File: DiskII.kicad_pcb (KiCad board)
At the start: 2 copper layers, 100 x 77.5 mm, 35 parts, among them J1 Apple II Expansion Slot, J2 DRIVE 2, J3 DRIVE 1, Q1 2N3906, Q2 MPSU51, Q3 MPSU51

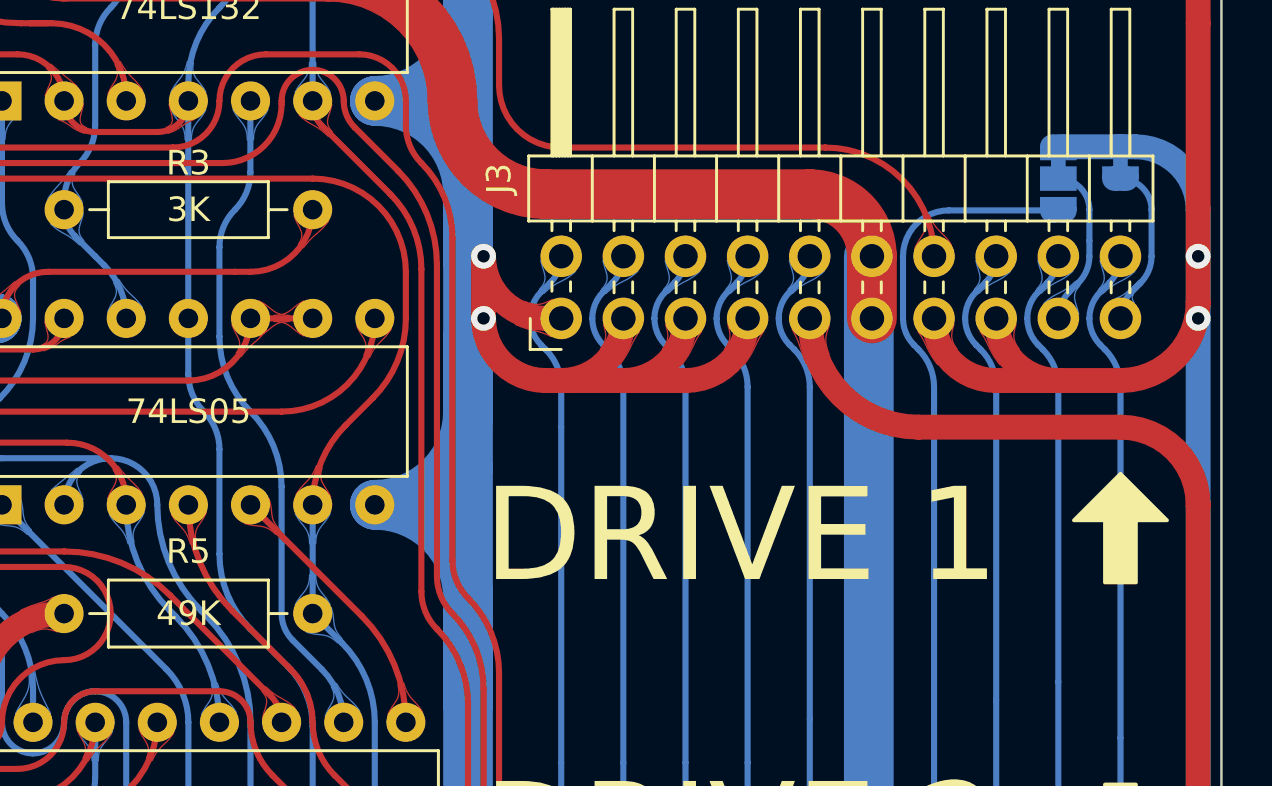
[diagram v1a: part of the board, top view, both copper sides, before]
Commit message: jumper to put WPROT on pin 19
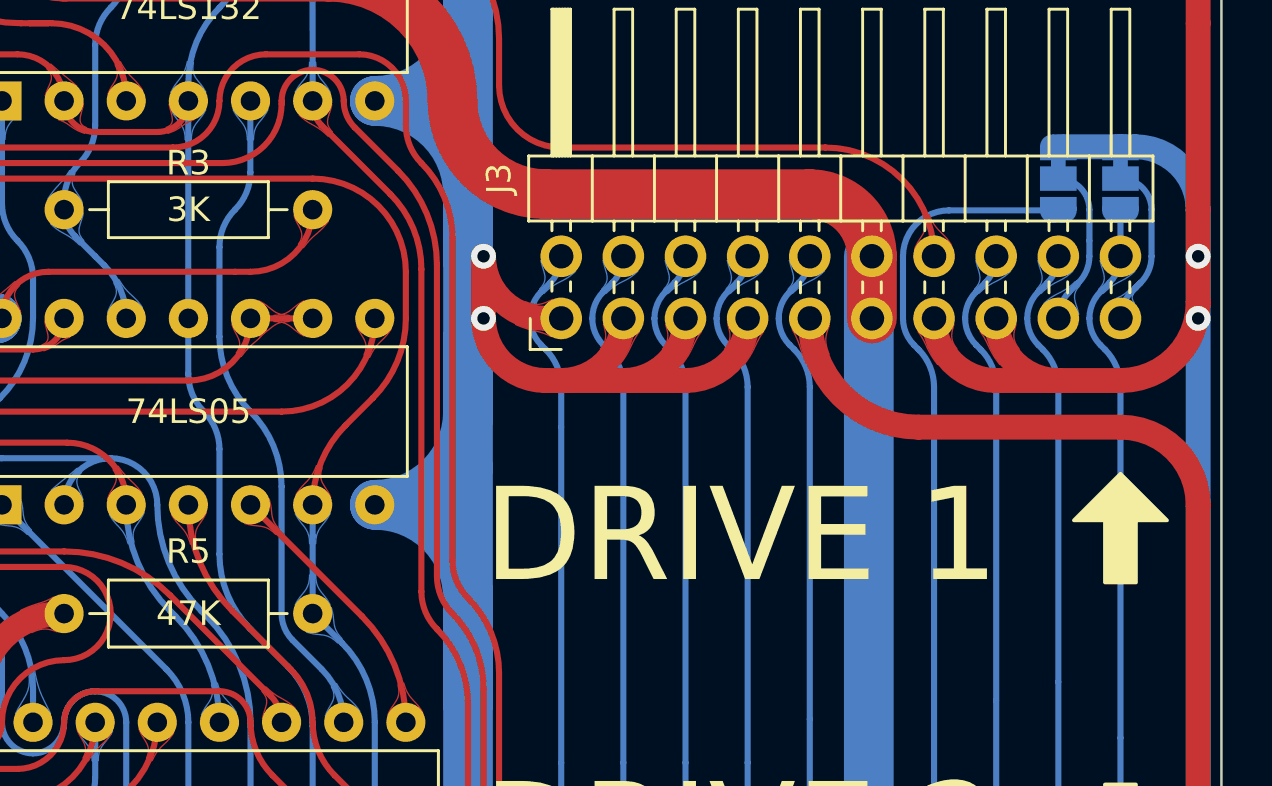
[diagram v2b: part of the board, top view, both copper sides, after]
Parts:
- JP19: footprint Jumper:SolderJumper-2_P1.3mm_Bridged_RoundedPad1.0x1.5mm -> Jumper:SolderJumper-3_P1.3mm_Bridged12_RoundedPad1.0x1.5mm
- R5: value 49K -> 47K
- moved JP19 0.65 mm to (207.0, 78.1)
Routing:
- net /W PROT: track 112.9 -> 114.7 mm

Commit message: starting rev 2
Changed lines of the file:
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@@
   (paper "A4")
   (title_block
-    (rev "1")
+    (rev "2")
   )
   (layers
